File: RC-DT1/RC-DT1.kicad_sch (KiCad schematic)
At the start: 10 parts

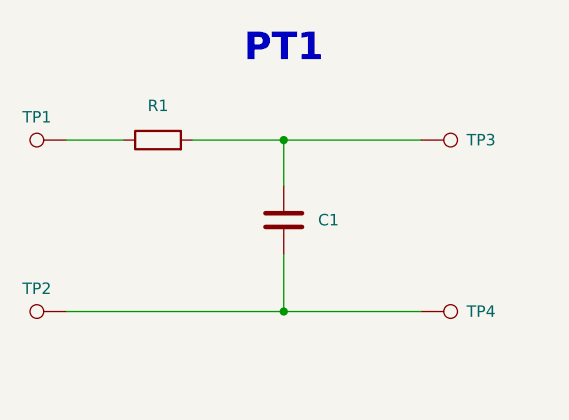
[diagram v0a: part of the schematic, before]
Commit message: DT1 added
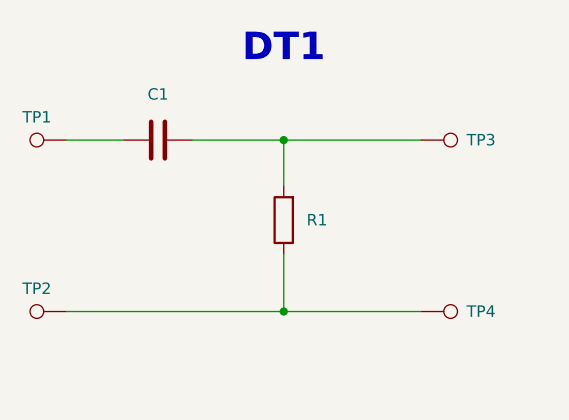
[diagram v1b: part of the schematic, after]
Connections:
- net at R1.1: now also TP2.1, TP4.1; no longer TP1.1
- net at R1.2, TP3.1: now also C1.2; no longer C1.1
- new net: C1.1, TP1.1
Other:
- note added: "DT1"
- note removed: "PT1"
- moved on the sheet: C1, R1
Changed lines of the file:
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@@
 	(generator_version "10.0")
 	(paper "A4")
-	(text "PT1"
+	(text "DT1"
 		(exclude_from_sim no)
 		(at 137.16 67.31 0)
@@
 		)
 		(instances
-			(project "RC-PT1"
+			(project "RC-DT1"
 				(path "/516af16e-4df2-44b9-98db-abada191c38c"
 					(reference "H3")
@@
 	(symbol
 		(lib_id "Device:R")
-		(at 123.19 77.47 90)
+		(at 137.16 86.36 180)
 		(unit 1)
 		(body_style 1)
@@
 		(fields_autoplaced yes)
 		(property "Reference" "R1"
-			(at 123.19 73.66 90)
-			(show_name no)
-			(do_not_autoplace no)
-			(effects
-				(font
-					(size 1.27 1.27)
-				)
+			(at 139.7 86.3599 0)
+			(show_name no)
+			(do_not_autoplace no)
+			(effects
+				(font
+					(size 1.27 1.27)
+				)
+				(justify right)
 			)
 		)
 		(property "Value" "R"
-			(at 123.19 73.66 90)
+			(at 133.35 86.36 90)
 			(hide yes)
 			(show_name no)
@@
 		)
 		(property "Footprint" "Resistor_THT:R_Axial_DIN0207_L6.3mm_D2.5mm_P10.16mm_Horizontal"
-			(at 123.19 79.248 90)
-			(hide yes)
-			(show_name no)
-			(do_not_autoplace no)
-			(effects
-				(font
-					(size 1.27 1.27)
-				)
-			)
-		)
-		(property "Datasheet" ""
-			(at 123.19 77.47 0)
+			(at 138.938 86.36 90)
+			(hide yes)
+			(show_name no)
+			(do_not_autoplace no)
+			(effects
+				(font
+					(size 1.27 1.27)
+				)
+			)
+		)
+		(property "Datasheet" ""
+			(at 137.16 86.36 0)
 			(hide yes)
 			(show_name no)
@@
 		)
 		(property "Description" "Resistor"
-			(at 123.19 77.47 0)
+			(at 137.16 86.36 0)
 			(hide yes)
 			(show_name no)
@@
 		)
 		(instances
-			(project "RC-PT1"
+			(project "RC-DT1"
 				(path "/516af16e-4df2-44b9-98db-abada191c38c"
 					(reference "R1")
@@
 		)
 		(instances
-			(project "RC-PT1"
+			(project "RC-DT1"
 				(path "/516af16e-4df2-44b9-98db-abada191c38c"
 					(reference "H4")
@@
 		)
 		(instances
-			(project "RC-PT1"
+			(project "RC-DT1"
 				(path "/516af16e-4df2-44b9-98db-abada191c38c"
 					(reference "TP2")
@@
 		)
 		(instances
-			(project "RC-PT1"
+			(project "RC-DT1"
 				(path "/516af16e-4df2-44b9-98db-abada191c38c"
 					(reference "TP4")
@@
 		)
 		(instances
-			(project "RC-PT1"
+			(project "RC-DT1"
 				(path "/516af16e-4df2-44b9-98db-abada191c38c"
 					(reference "TP3")
@@
 		)
 		(instances
-			(project "RC-PT1"
+			(project "RC-DT1"
 				(path "/516af16e-4df2-44b9-98db-abada191c38c"
 					(reference "H1")
@@
 		)
 		(instances
-			(project "RC-PT1"
+			(project "RC-DT1"
 				(path "/516af16e-4df2-44b9-98db-abada191c38c"
 					(reference "TP1")
@@
 		)
 		(instances
-			(project "RC-PT1"
+			(project "RC-DT1"
 				(path "/516af16e-4df2-44b9-98db-abada191c38c"
 					(reference "H2")
@@
 	(symbol
 		(lib_id "Device:C")
-		(at 137.16 86.36 0)
+		(at 123.19 77.47 90)
 		(unit 1)
 		(body_style 1)
@@
 		(fields_autoplaced yes)
 		(property "Reference" "C1"
-			(at 140.97 86.3599 0)
-			(show_name no)
-			(do_not_autoplace no)
-			(effects
-				(font
-					(size 1.27 1.27)
-				)
-				(justify left)
+			(at 123.19 72.39 90)
+			(show_name no)
+			(do_not_autoplace no)
+			(effects
+				(font
+					(size 1.27 1.27)
+				)
 			)
 		)
 		(property "Value" "C"
-			(at 140.97 87.6299 0)
+			(at 124.4599 73.66 0)
 			(hide yes)
 			(show_name no)
@@
 		)
 		(property "Footprint" "Capacitor_THT:C_Rect_L7.2mm_W5.0mm_P5.00mm"
-			(at 138.1252 90.17 0)
-			(hide yes)
-			(show_name no)
-			(do_not_autoplace no)
-			(effects
-				(font
-					(size 1.27 1.27)
-				)
-			)
-		)
-		(property "Datasheet" ""
-			(at 137.16 86.36 0)
+			(at 127 76.5048 0)
+			(hide yes)
+			(show_name no)
+			(do_not_autoplace no)
+			(effects
+				(font
+					(size 1.27 1.27)
+				)
+			)
+		)
+		(property "Datasheet" ""
+			(at 123.19 77.47 0)
 			(hide yes)
 			(show_name no)
@@
 		)
 		(property "Description" "Unpolarized capacitor"
-			(at 137.16 86.36 0)
+			(at 123.19 77.47 0)
 			(hide yes)
 			(show_name no)
@@
 		)
 		(instances
-			(project "RC-PT1"
+			(project "RC-DT1"
 				(path "/516af16e-4df2-44b9-98db-abada191c38c"
 					(reference "C1")
